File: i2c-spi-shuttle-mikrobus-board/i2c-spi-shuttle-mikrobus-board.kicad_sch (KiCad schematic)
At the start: 0 parts

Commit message: first version of i2c-spi-shuttle-mikrobus-board
TODO:
* purpose of board on silkscreen
* some pin explanations on silkscreen (probably rear)
* check if shuttle connector is oriented correctly!
  (MikroE schematics are inconsistent, test with multimeter)
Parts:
- added C1, C2: 100nF, Capacitor_SMD:C_0402_1005Metric, symbol Device:C_Small
- added D1: PWR, LED_SMD:LED_0805_2012Metric, symbol Device:LED
- added J1, J2: Conn_01x08, Connector_PinHeader_2.54mm:PinHeader_1x08_P2.54mm_Vertical, symbol Connector_Generic:Conn_01x08
- added J3: Shuttle, Connector_PinHeader_1.27mm_LowProfile:CNC_3221-16-0300-00, symbol Connector_Generic:Conn_02x08_Odd_Even
- added JP1: Jumper_2_Open, Connector_PinHeader_2.54mm:PinHeader_1x02_P2.54mm_Vertical, symbol Jumper:Jumper_2_Open
- added R1: 33Ω, Resistor_SMD:R_0603_1608Metric, symbol Device:R
- added R2, R3, R4: 4.7kΩ, Resistor_SMD:R_0402_1005Metric, symbol Device:R
- added SW1: ADDR, Button_Switch_SMD:Nidec_Copal_CAS-D20A, symbol Switch:SW_DPDT_x2
- added U1: SC18IS606PW, Package_SO:TSSOP-16_4.4x5mm_P0.65mm, symbol Interface:SC18IS606PW
- added U2: PCAL9538APW, Package_SO:TSSOP-16_4.4x5mm_P0.65mm, symbol Interface_Expansion:PCA9538D
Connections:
- new net: D1.1 (K), R1.1
- new net +3.3V: C1.1, C2.1, D1.2 (A), J1.7 (Pin_7), J3.13 (Pin_13), R2.1, R3.1, R4.1, SW1.1 (A), SW1.4 (A), U1.12 (V_{DD}), U1.15 (V_{DD}), U2.16 (VDD)
- new net A0: SW1.2 (B), U1.7 (A0), U2.1 (A0)
- new net A1: SW1.5 (B), U1.6 (A1), U2.2 (A1)
- new net GND: C1.2, C2.2, J1.8 (Pin_8), J2.8 (Pin_8), J3.15 (Pin_15), J3.16 (Pin_16), R1.2, SW1.3 (C), SW1.6 (C), U1.13 (V_{SS}), U1.5 (A2), U2.8 (VSS)
- new net IN_+5V: J2.7 (Pin_7)
- new net IN_AN: J1.1 (Pin_1)
- new net IN_CIPO: J1.5 (Pin_5)
- new net IN_COPI: J1.6 (Pin_6)
- new net IN_PWM: J2.1 (Pin_1)
- new net IN_RX: J2.3 (Pin_3)
- new net IN_SCK: J1.4 (Pin_4)
- new net IN_TX: J2.4 (Pin_4)
- new net IN_~{CS}: J1.3 (Pin_3)
- new net IN_~{INT}: J2.2 (Pin_2), JP1.1 (A)
- new net IN_~{RST}: J1.2 (Pin_2), R4.2, U1.4 (~{RESET}), U2.3 (~{RESET})
- new net MID_~{INT}: JP1.2 (B), U1.3 (~{INT}), U2.13 (~{INT})
- new net OUT_+5V: J3.14 (Pin_14)
- new net OUT_AN: J3.1 (Pin_1), U2.6 (IO2)
- new net OUT_CIPO: J3.9 (Pin_9), U1.14 (MISO)
- new net OUT_COPI: J3.11 (Pin_11), U1.10 (MOSI)
- new net OUT_PWM: J3.2 (Pin_2), U2.9 (IO4)
- new net OUT_RX: J3.6 (Pin_6)
- new net OUT_SCK: J3.7 (Pin_7), U1.11 (SPICLK)
- new net OUT_TX: J3.8 (Pin_8)
- new net OUT_~{CS}: J3.5 (Pin_5), U1.9 (~{SS0}/GPIO0)
- new net OUT_~{INT}: J3.4 (Pin_4), U2.10 (IO5)
- new net OUT_~{RST}: J3.3 (Pin_3), U2.7 (IO3)
- new net SCL: J2.5 (Pin_5), J3.10 (Pin_10), R2.2, U1.2 (SCL), U2.14 (SCL)
- new net SDA: J2.6 (Pin_6), J3.12 (Pin_12), R3.2, U1.1 (SDA), U2.15 (SDA)
- no-connect marks 0 -> 18
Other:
- note added: "FIXME: Check orientation!"
- note added: "I^{2}C addr: 01010xy"
- note added: "I^{2}C addr: 11100xy"
- note added: "min. 24Ω"

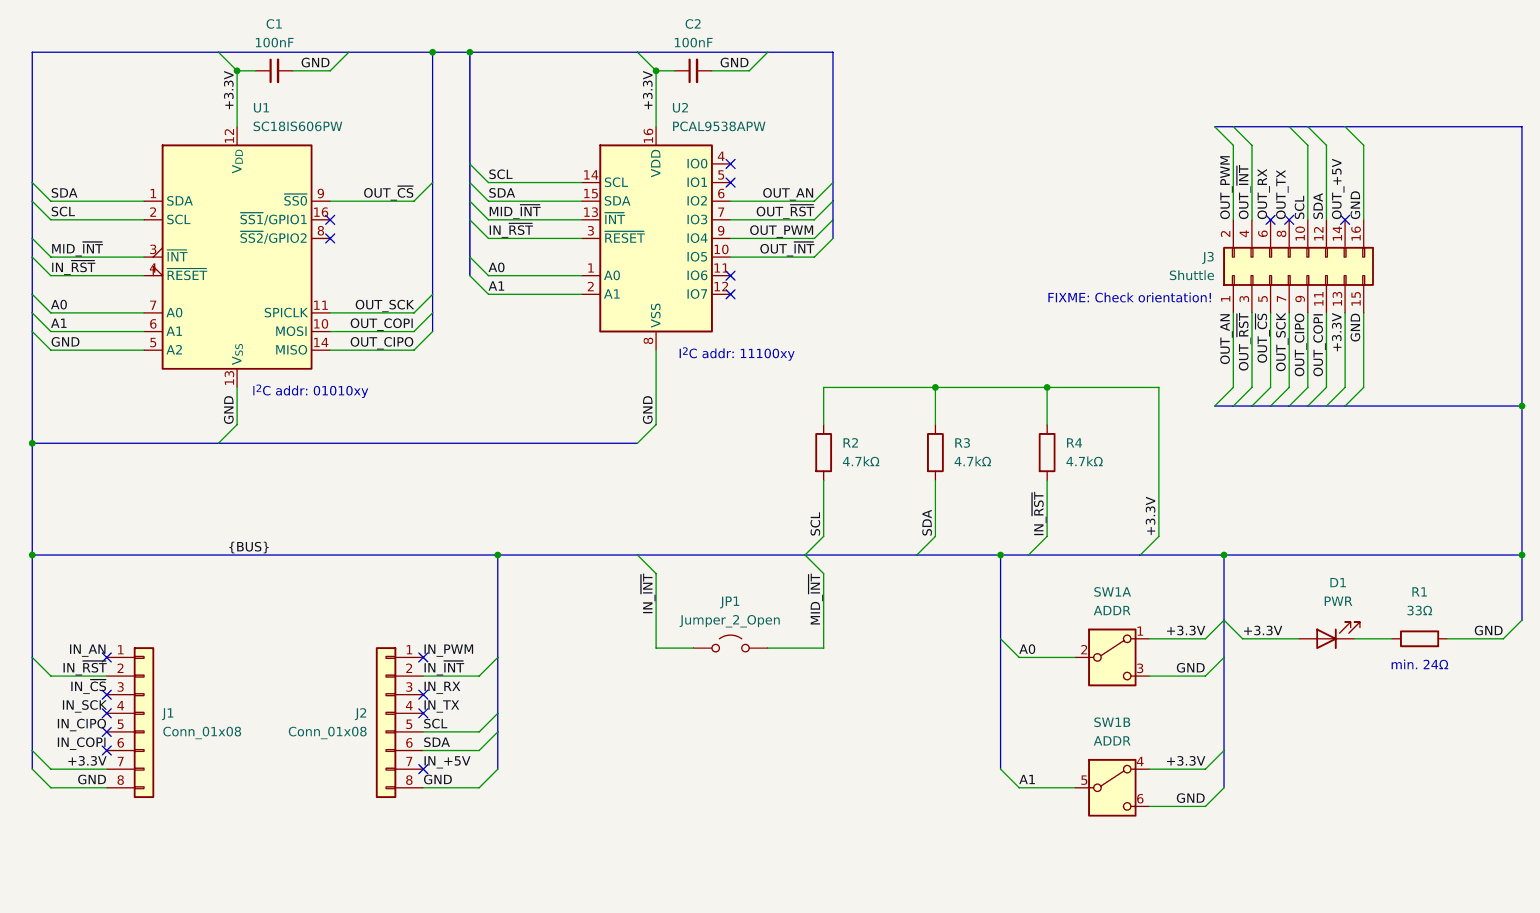
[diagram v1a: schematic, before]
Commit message: fix shuttle pinout in schematic, clear PCB of tracks (we must reroute)
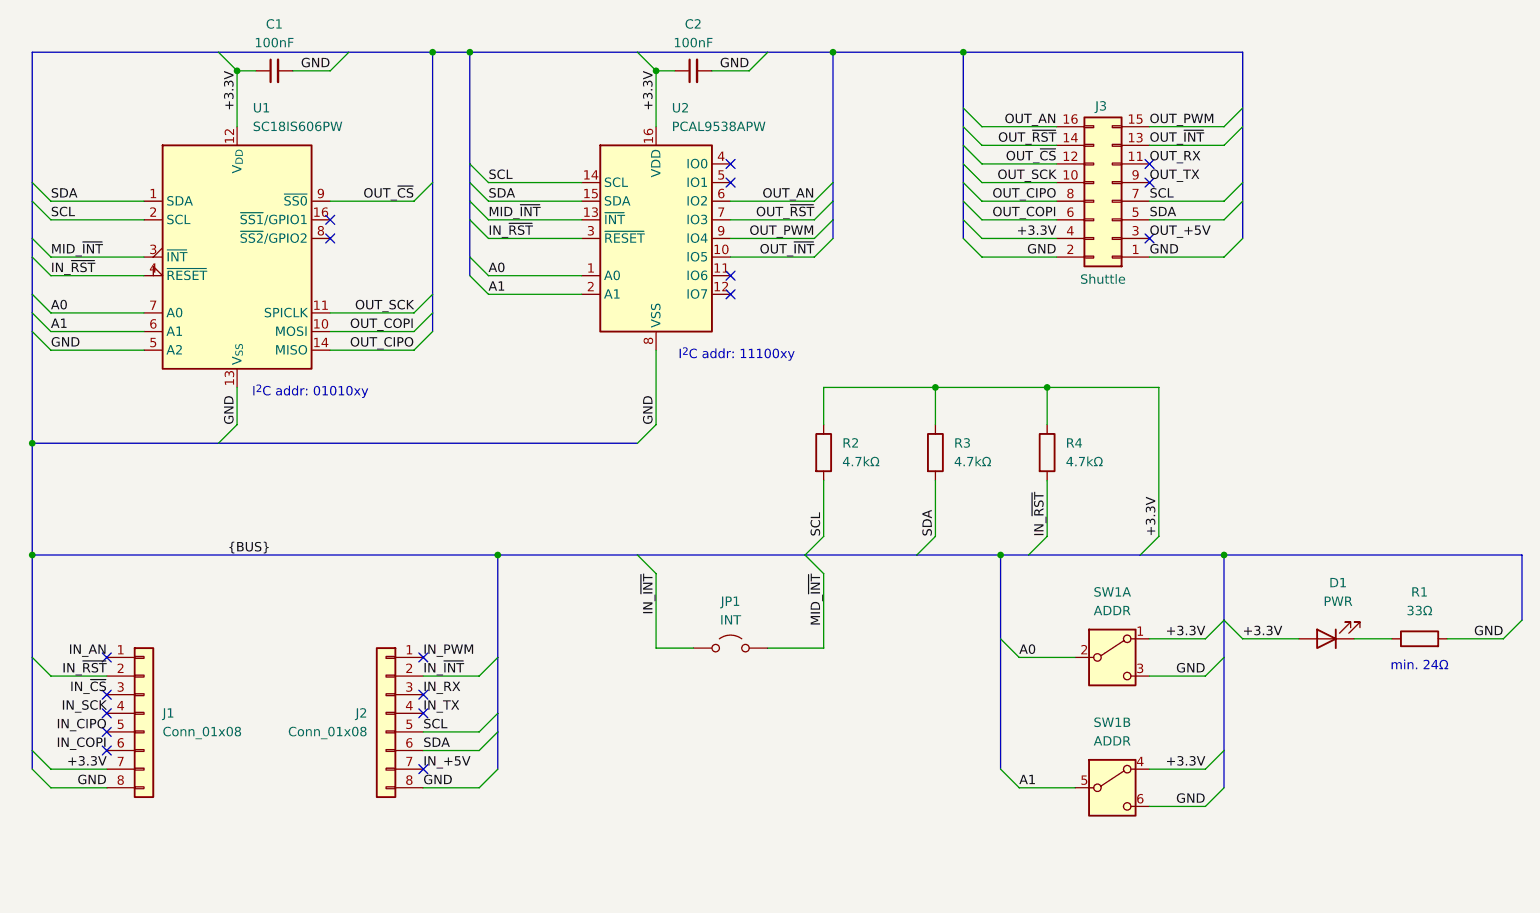
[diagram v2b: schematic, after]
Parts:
- JP1: value Jumper_2_Open -> INT
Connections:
- net +3.3V: now also J3.4 (Pin_4); no longer J3.13 (Pin_13)
- net GND: now also J3.1 (Pin_1), J3.2 (Pin_2); no longer J3.15 (Pin_15), J3.16 (Pin_16)
- net OUT_+5V: now also J3.3 (Pin_3); no longer J3.14 (Pin_14)
- net OUT_AN: now also J3.16 (Pin_16); no longer J3.1 (Pin_1)
- net OUT_CIPO: now also J3.8 (Pin_8); no longer J3.9 (Pin_9)
- net OUT_COPI: now also J3.6 (Pin_6); no longer J3.11 (Pin_11)
- net OUT_PWM: now also J3.15 (Pin_15); no longer J3.2 (Pin_2)
- net OUT_RX: now also J3.11 (Pin_11); no longer J3.6 (Pin_6)
- net OUT_SCK: now also J3.10 (Pin_10); no longer J3.7 (Pin_7)
- net OUT_TX: now also J3.9 (Pin_9); no longer J3.8 (Pin_8)
- net OUT_~{CS}: now also J3.12 (Pin_12); no longer J3.5 (Pin_5)
- net OUT_~{INT}: now also J3.13 (Pin_13); no longer J3.4 (Pin_4)
- net OUT_~{RST}: now also J3.14 (Pin_14); no longer J3.3 (Pin_3)
- net SCL: now also J3.7 (Pin_7); no longer J3.10 (Pin_10)
- net SDA: now also J3.5 (Pin_5); no longer J3.12 (Pin_12)
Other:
- note removed: "FIXME: Check orientation!"
- moved on the sheet: J3

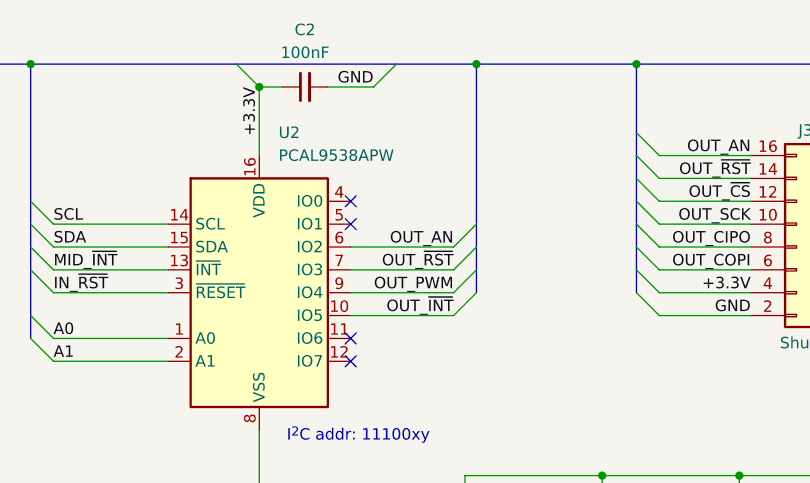
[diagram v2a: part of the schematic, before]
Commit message: route the I2C-SPI Shuttle board now that the pinout is fixed
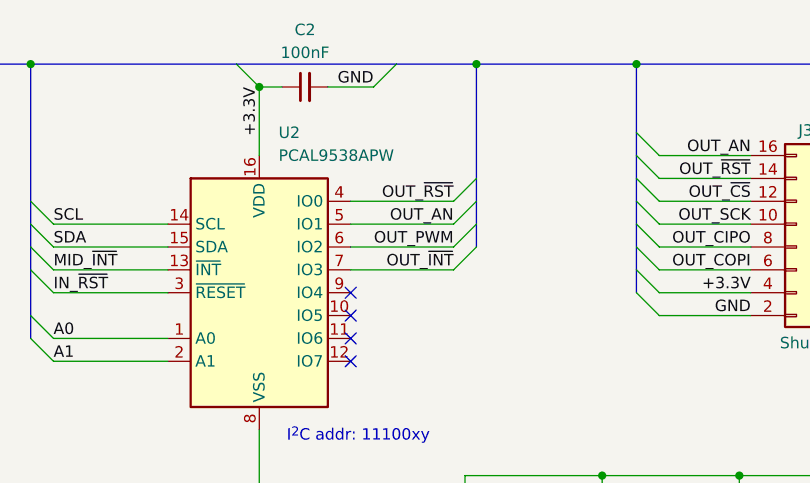
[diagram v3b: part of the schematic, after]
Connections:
- net OUT_AN: now also U2.5 (IO1); no longer U2.6 (IO2)
- net OUT_PWM: now also U2.6 (IO2); no longer U2.9 (IO4)
- net OUT_~{INT}: now also U2.7 (IO3); no longer U2.10 (IO5)
- net OUT_~{RST}: now also U2.4 (IO0); no longer U2.7 (IO3)
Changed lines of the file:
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@@
+	)
+	(no_connect
+		(at 144.78 72.39)
 	)
 	(no_connect
@@
 	)
 	(no_connect
-		(at 144.78 64.77)
+		(at 144.78 80.01)
 	)
 	(no_connect
-		(at 144.78 80.01)
+		(at 144.78 74.93)
 	)
 	(no_connect
@@
 	)
 	(no_connect
-		(at 144.78 62.23)
-	)
-	(no_connect
 		(at 102.87 137.16)
 	)
@@
 	)
 	(bus_entry
-		(at 158.75 69.85)
+		(at 158.75 62.23)
 		(size -2.54 2.54)
 		(stroke
@@
 	)
 	(bus_entry
-		(at 158.75 72.39)
-		(size -2.54 2.54)
-		(stroke
-			(width 0)
-			(type default)
-		)
-	)
-	(bus_entry
 		(at 176.53 59.69)
 		(size 2.54 2.54)
@@
 	)
 	(bus_entry
+		(at 158.75 59.69)
+		(size -2.54 2.54)
+		(stroke
+			(width 0)
+			(type default)
+		)
+	)
+	(bus_entry
 		(at 214.63 72.39)
 		(size -2.54 2.54)
@@
 	(bus
 		(pts
+			(xy 158.75 59.69) (xy 158.75 62.23)
+		)
+		(stroke
+			(width 0)
+			(type default)
+		)
+	)
+	(bus
+		(pts
 			(xy 176.53 54.61) (xy 176.53 57.15)
 		)
@@
 	(bus
 		(pts
-			(xy 158.75 69.85) (xy 158.75 72.39)
-		)
-		(stroke
-			(width 0)
-			(type default)
-		)
-	)
-	(bus
-		(pts
 			(xy 113.03 139.7) (xy 113.03 137.16)
 		)
@@
 	(bus
 		(pts
-			(xy 158.75 46.99) (xy 158.75 64.77)
+			(xy 158.75 46.99) (xy 158.75 59.69)
 		)
 		(stroke
@@
 	(wire
 		(pts
+			(xy 144.78 62.23) (xy 156.21 62.23)
+		)
+		(stroke
+			(width 0)
+			(type default)
+		)
+	)
+	(wire
+		(pts
 			(xy 90.17 67.31) (xy 101.6 67.31)
 		)
@@
 	(bus
 		(pts
-			(xy 158.75 67.31) (xy 158.75 69.85)
-		)
-		(stroke
-			(width 0)
-			(type default)
-		)
-	)
-	(bus
-		(pts
 			(xy 49.53 129.54) (xy 49.53 142.24)
 		)
@@
 	(wire
 		(pts
-			(xy 144.78 72.39) (xy 156.21 72.39)
+			(xy 144.78 64.77) (xy 156.21 64.77)
 		)
 		(stroke
@@
 		)
 	)
-	(wire
-		(pts
-			(xy 144.78 74.93) (xy 156.21 74.93)
+	(bus
+		(pts
+			(xy 158.75 62.23) (xy 158.75 64.77)
 		)
 		(stroke
@@
 	)
 	(label "OUT_~{RST}"
+		(at 156.21 62.23 180)
+		(effects
+			(font
+				(size 1.27 1.27)
+			)
+			(justify right bottom)
+		)
+	)
+	(label "OUT_~{INT}"
 		(at 156.21 69.85 180)
-		(effects
-			(font
-				(size 1.27 1.27)
-			)
-			(justify right bottom)
-		)
-	)
-	(label "OUT_~{INT}"
-		(at 156.21 74.93 180)
 		(effects
 			(font
@@
 	)
 	(label "OUT_AN"
-		(at 156.21 67.31 180)
+		(at 156.21 64.77 180)
 		(effects
 			(font
@@
 	)
 	(label "OUT_PWM"
-		(at 156.21 72.39 180)
-		(effects
-			(font
+		(at 156.21 67.31 180)
+		(effects
+			(font
